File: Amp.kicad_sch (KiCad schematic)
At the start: 8 parts, among them U1 LM317_SOT-223

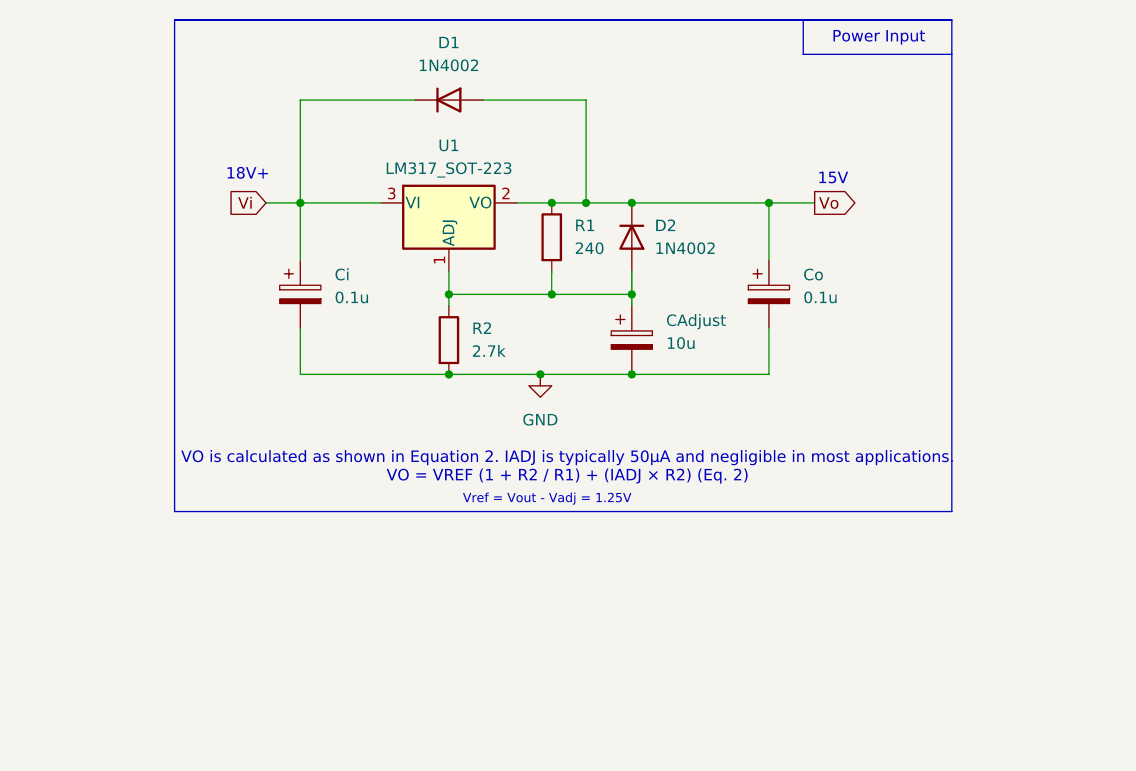
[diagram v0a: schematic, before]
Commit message: Finish Power Section & Make multisheet schema
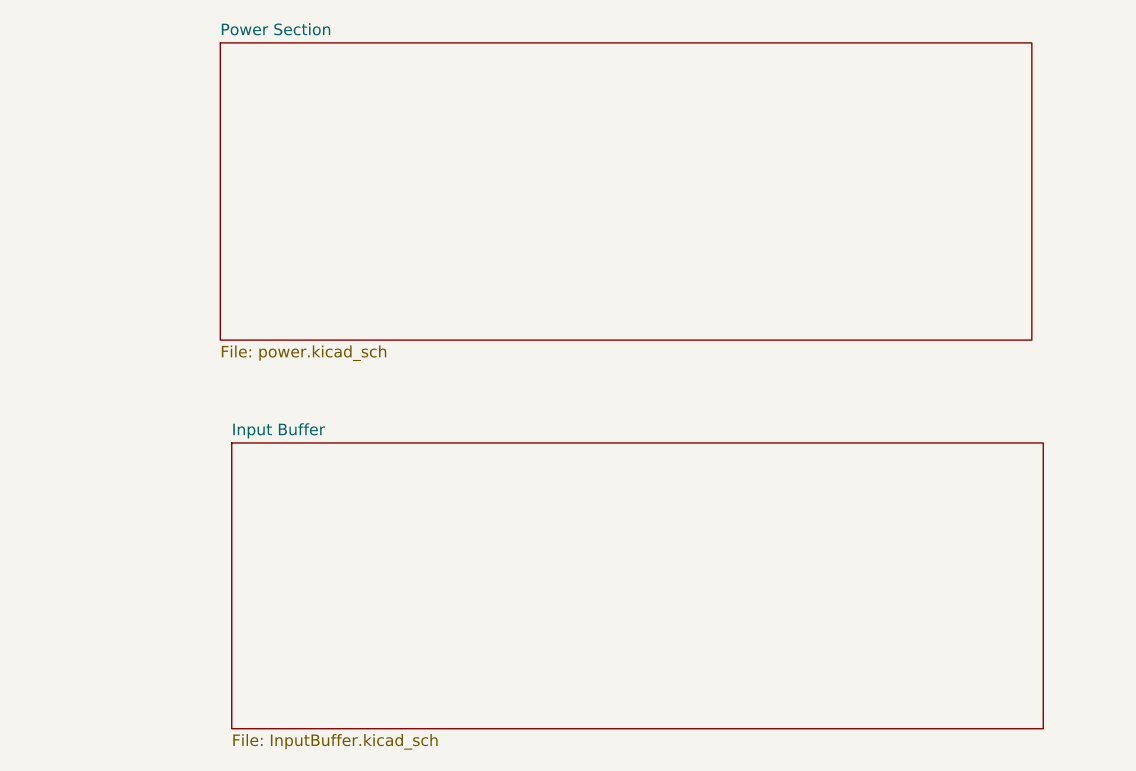
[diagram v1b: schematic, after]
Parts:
- removed CAdjust: 10u, symbol Device:C_Polarized
- removed Ci, Co: 0.1u, symbol Device:C_Polarized
- removed D1, D2: 1N4002, Diode_THT:D_DO-41_SOD81_P10.16mm_Horizontal, symbol Diode:1N4002
- removed R1: 240, symbol Device:R
- removed R2: 2.7k, symbol Device:R
- removed U1: LM317_SOT-223, Package_TO_SOT_SMD:SOT-223-3_TabPin2, symbol Regulator_Linear:LM317_SOT-223
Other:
- added sheet Input Buffer (InputBuffer.kicad_sch)
- added sheet Power Section (power.kicad_sch)
- note removed: "15V"
- note removed: "18V+"
- note removed: "Power Input"
- note removed: "VO is calculated as shown in Equation 2. IADJ is typically 50µA and negligible in most applications. VO = VREF (1 + R2 / R1) + (IADJ × R2) (Eq. 2)"
- note removed: "Vref = Vout - Vadj = 1.25V"
- title: Headphone Amplifier -> Headphone Amplifier 

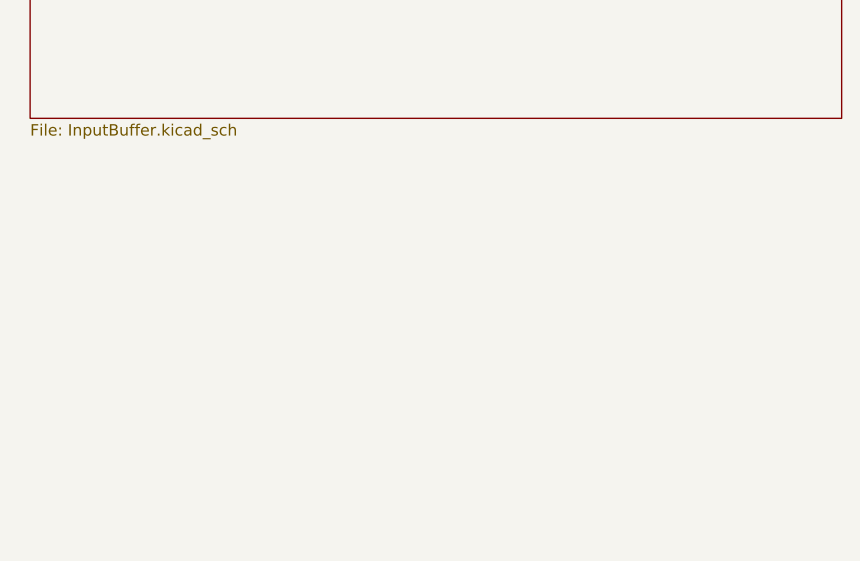
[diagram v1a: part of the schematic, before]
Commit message: Finish Input Buffer & Add Volume Control Sheet
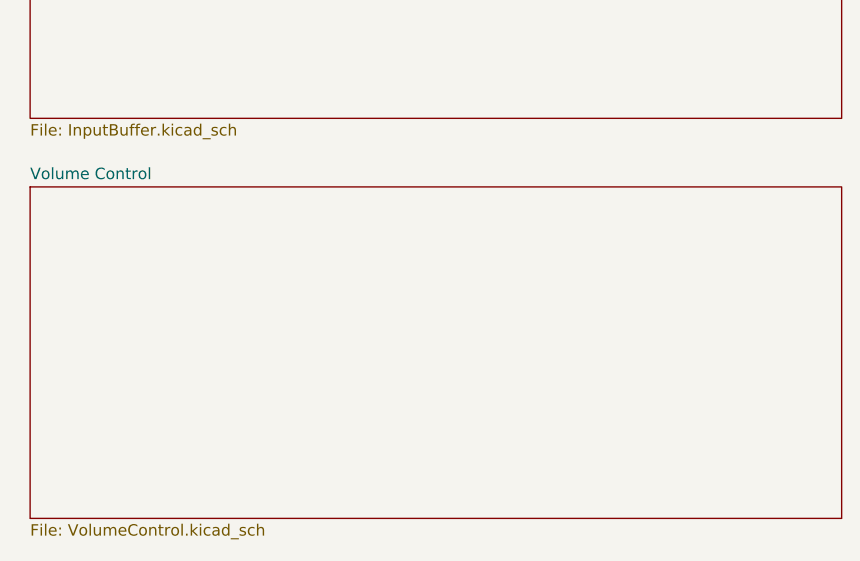
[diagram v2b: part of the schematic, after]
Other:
- added sheet Volume Control (VolumeControl.kicad_sch)
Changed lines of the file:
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@@
+	)
+	(sheet
+		(at 24.13 102.87)
+		(size 90.17 36.83)
+		(exclude_from_sim no)
+		(in_bom yes)
+		(on_board yes)
+		(dnp no)
+		(fields_autoplaced yes)
+		(stroke
+			(width 0.1524)
+			(type solid)
+		)
+		(fill
+			(color 0 0 0 0.0000)
+		)
+		(property "Sheetname" "Volume Control"
+			(at 24.13 102.1584 0)
+			(effects
+				(font
+					(size 1.27 1.27)
+				)
+				(justify left bottom)
+			)
+		)
+		(property "Sheetfile" "VolumeControl.kicad_sch"
+			(at 24.13 140.2846 0)
+			(effects
+				(font
+					(size 1.27 1.27)
+				)
+				(justify left top)
+			)
+		)
+		(instances
+			(project "Amp"
+				(path "/5faae81d-f66a-438b-a97a-07010798add6"
+					(page "4")
+				)
+			)
+		)
 	)
 	(sheet

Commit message: Complete Volume Control
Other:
- added sheet Output Stage (Output.kicad_sch)
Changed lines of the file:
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@@
+	)
+	(sheet
+		(at 137.16 20.32)
+		(size 115.57 34.29)
+		(exclude_from_sim no)
+		(in_bom yes)
+		(on_board yes)
+		(dnp no)
+		(fields_autoplaced yes)
+		(stroke
+			(width 0.1524)
+			(type solid)
+		)
+		(fill
+			(color 0 0 0 0.0000)
+		)
+		(property "Sheetname" "Output Stage"
+			(at 137.16 19.6084 0)
+			(effects
+				(font
+					(size 1.27 1.27)
+				)
+				(justify left bottom)
+			)
+		)
+		(property "Sheetfile" "Output.kicad_sch"
+			(at 137.16 55.1946 0)
+			(effects
+				(font
+					(size 1.27 1.27)
+				)
+				(justify left top)
+			)
+		)
+		(instances
+			(project "Amp"
+				(path "/5faae81d-f66a-438b-a97a-07010798add6"
+					(page "5")
+				)
+			)
+		)
 	)
 	(sheet

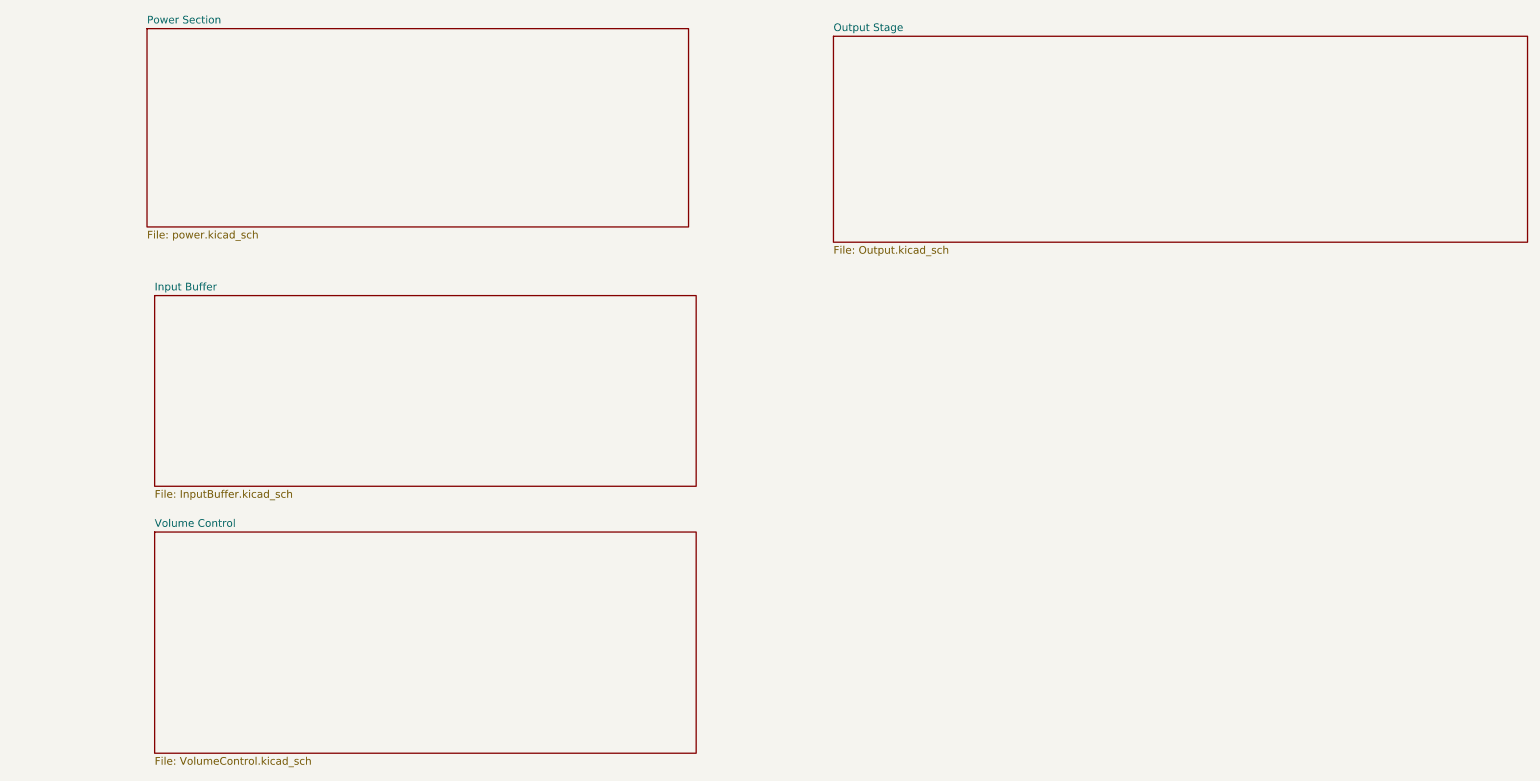
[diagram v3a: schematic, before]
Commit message: Finish Output Stage & Finish Schematic
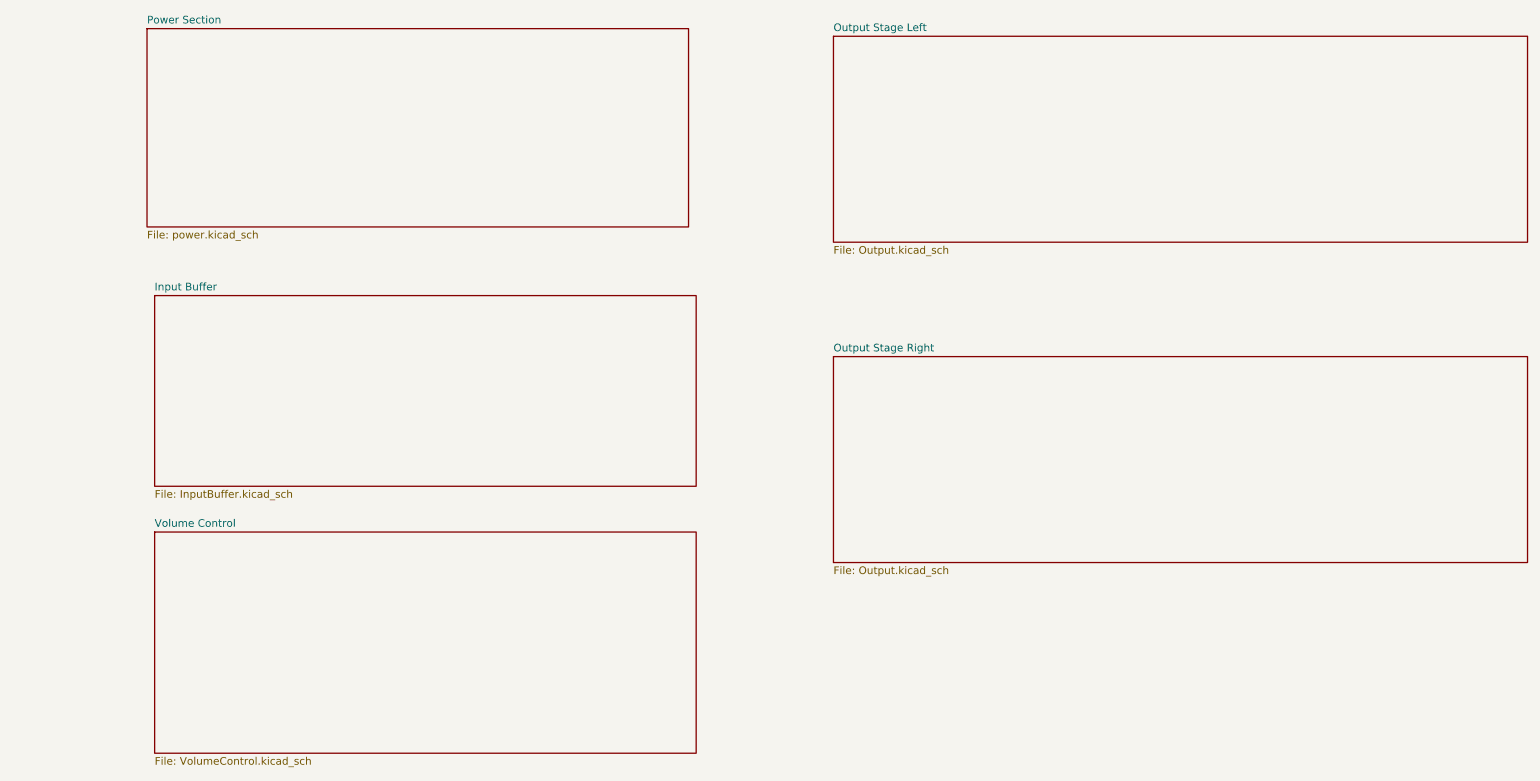
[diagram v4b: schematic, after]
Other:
- sheet Output Stage renamed Output Stage Left
- added sheet Output Stage Right (Output.kicad_sch)
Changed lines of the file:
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@@
 			(color 0 0 0 0.0000)
 		)
-		(property "Sheetname" "Output Stage"
+		(property "Sheetname" "Output Stage Left"
 			(at 137.16 19.6084 0)
 			(effects
@@
 				)
 			)
+		)
+	)
+	(sheet
+		(at 137.16 73.66)
+		(size 115.57 34.29)
+		(exclude_from_sim no)
+		(in_bom yes)
+		(on_board yes)
+		(dnp no)
+		(fields_autoplaced yes)
+		(stroke
+			(width 0.1524)
+			(type solid)
+		)
+		(fill
+			(color 0 0 0 0.0000)
+		)
+		(property "Sheetname" "Output Stage Right"
+			(at 137.16 72.9484 0)
+			(effects
+				(font
+					(size 1.27 1.27)
+				)
+				(justify left bottom)
+			)
+		)
+		(property "Sheetfile" "Output.kicad_sch"
+			(at 137.16 108.5346 0)
+			(effects
+				(font
+					(size 1.27 1.27)
+				)
+				(justify left top)
+			)
+		)
+		(instances
+			(project "Amp"
+				(path "/5faae81d-f66a-438b-a97a-07010798add6"
+					(page "6")
+				)
+			)

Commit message: Add inputs audio and power and correct errors
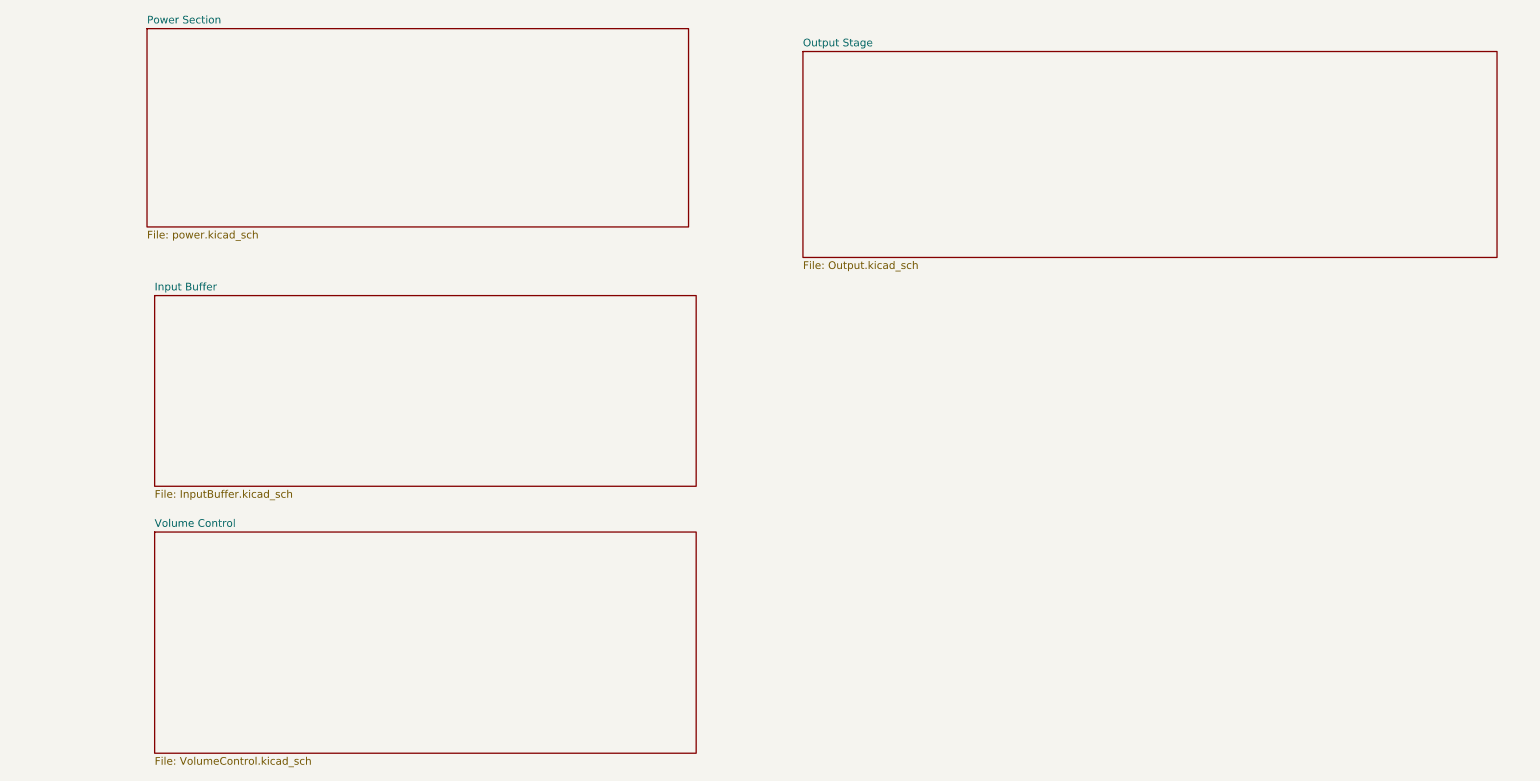
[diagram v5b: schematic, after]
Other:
- sheet Output Stage Right renamed Output Stage
- removed sheet Output Stage Left
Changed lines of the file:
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@@
 	)
 	(sheet
-		(at 137.16 20.32)
+		(at 132.08 22.86)
 		(size 115.57 34.29)
 		(exclude_from_sim no)
@@
 			(color 0 0 0 0.0000)
 		)
-		(property "Sheetname" "Output Stage Left"
-			(at 137.16 19.6084 0)
+		(property "Sheetname" "Output Stage"
+			(at 132.08 22.1484 0)
 			(effects
 				(font
@@
 		)
 		(property "Sheetfile" "Output.kicad_sch"
-			(at 137.16 55.1946 0)
+			(at 132.08 57.7346 0)
 			(effects
 				(font
-					(size 1.27 1.27)
-				)
-				(justify left top)
-			)
-		)
-		(instances
-			(project "Amp"
-				(path "/5faae81d-f66a-438b-a97a-07010798add6"
-					(page "5")
-				)
-			)
-		)
-	)
-	(sheet
-		(at 137.16 73.66)
-		(size 115.57 34.29)
-		(exclude_from_sim no)
-		(in_bom yes)
-		(on_board yes)
-		(dnp no)
-		(fields_autoplaced yes)
-		(stroke
-			(width 0.1524)
-			(type solid)
-		)
-		(fill
-			(color 0 0 0 0.0000)
-		)
-		(property "Sheetname" "Output Stage Right"
-			(at 137.16 72.9484 0)
-			(effects
-				(font
-					(size 1.27 1.27)
-				)
-				(justify left bottom)
-			)
-		)
-		(property "Sheetfile" "Output.kicad_sch"
-			(at 137.16 108.5346 0)
-			(effects
-				(font
